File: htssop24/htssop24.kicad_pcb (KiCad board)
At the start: 2 copper layers, 23.9 x 31.6 mm, 3 parts, among them J1 Conn_01x12, J2 Conn_02x12_Counter_Clockwise, J3 Conn_01x12

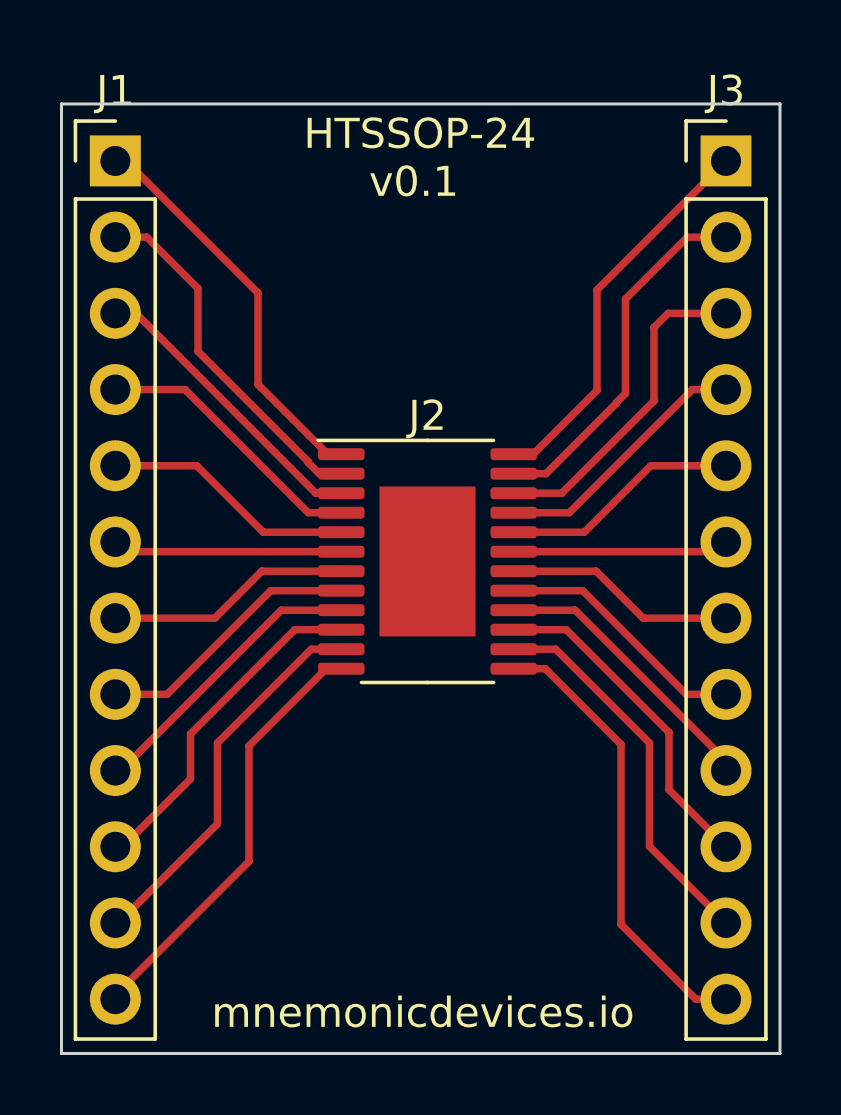
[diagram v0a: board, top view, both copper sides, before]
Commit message: gerber file for htssop24
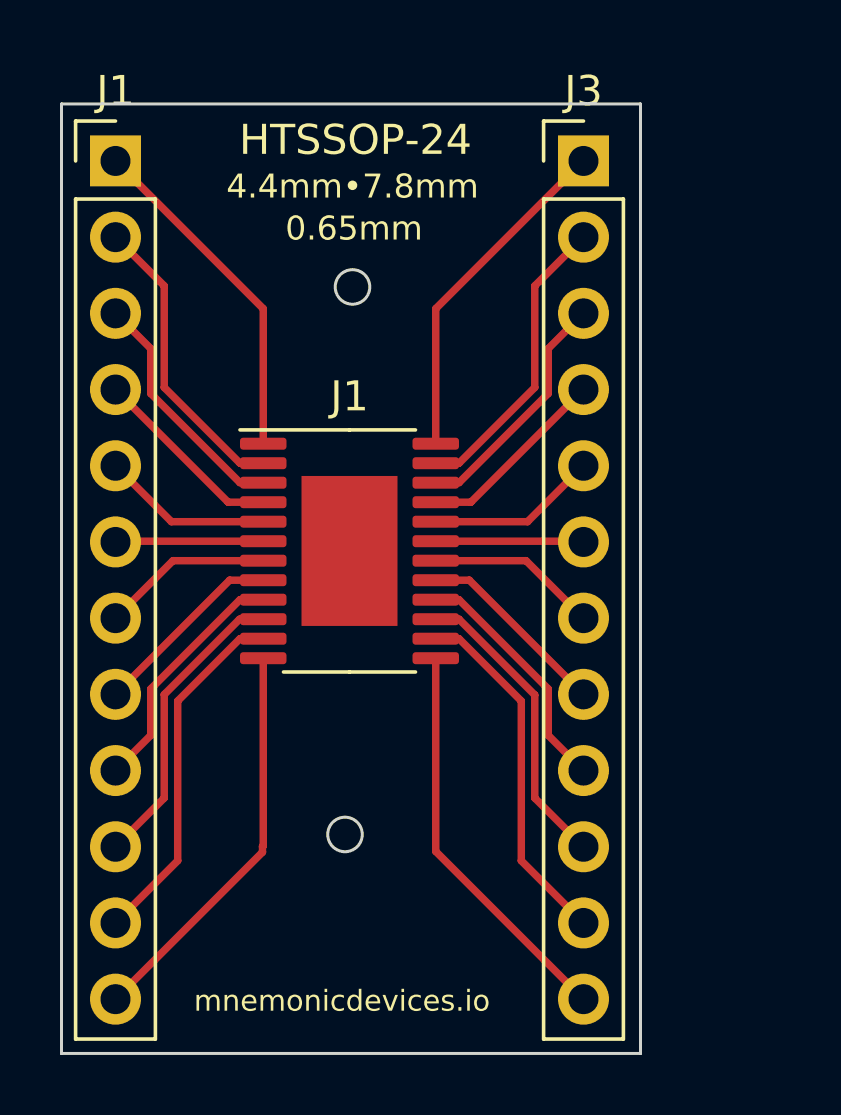
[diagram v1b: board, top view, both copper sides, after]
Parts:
- moved J3 4.75 mm to (29.5, 13.9)
- moved J1 2.62 mm to (21.7, 26.9)
- renumbered J2 to J1
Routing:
- net Net-(J1-Pad4): track 9.53 -> 6.48 mm
- net Net-(J1-Pad5): track 8.75 -> 5.70 mm
- net Net-(J1-Pad6): track 7.96 -> 4.94 mm
- net Net-(J1-Pad7): track 8.48 -> 5.72 mm
- net Net-(J1-Pad8): track 9.26 -> 6.50 mm
- net Net-(J2-Pad22): track 10.7 -> 8.14 mm
- net Net-(J1-Pad2): track 12.3 -> 10.0 mm
- net Net-(J1-Pad3): track 10.4 -> 8.14 mm
- net Net-(J1-Pad1): track 13.7 -> 11.5 mm
- net Net-(J2-Pad21): track 8.48 -> 6.48 mm
- net Net-(J2-Pad20): track 7.69 -> 5.70 mm
- net Net-(J2-Pad19): track 6.91 -> 4.94 mm
- net Net-(J1-Pad12): track 15.4 -> 13.4 mm
- net Net-(J2-Pad23): track 11.9 -> 10.0 mm
- net Net-(J1-Pad9): track 10.0 -> 8.19 mm
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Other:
- board size 23.9 x 31.6 mm -> 19.3 x 31.6 mm
- board text added: "0.65mm"
- board text added: "4.4mm•7.8mm"
- board text removed: "v0.1"
